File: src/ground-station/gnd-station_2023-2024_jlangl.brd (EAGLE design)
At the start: 114.3 x 54.3 mm, 9 parts, among them IC1 LM7805_TO220V, U1 ADAFRUIT_RFM95W_LORA_RADIO

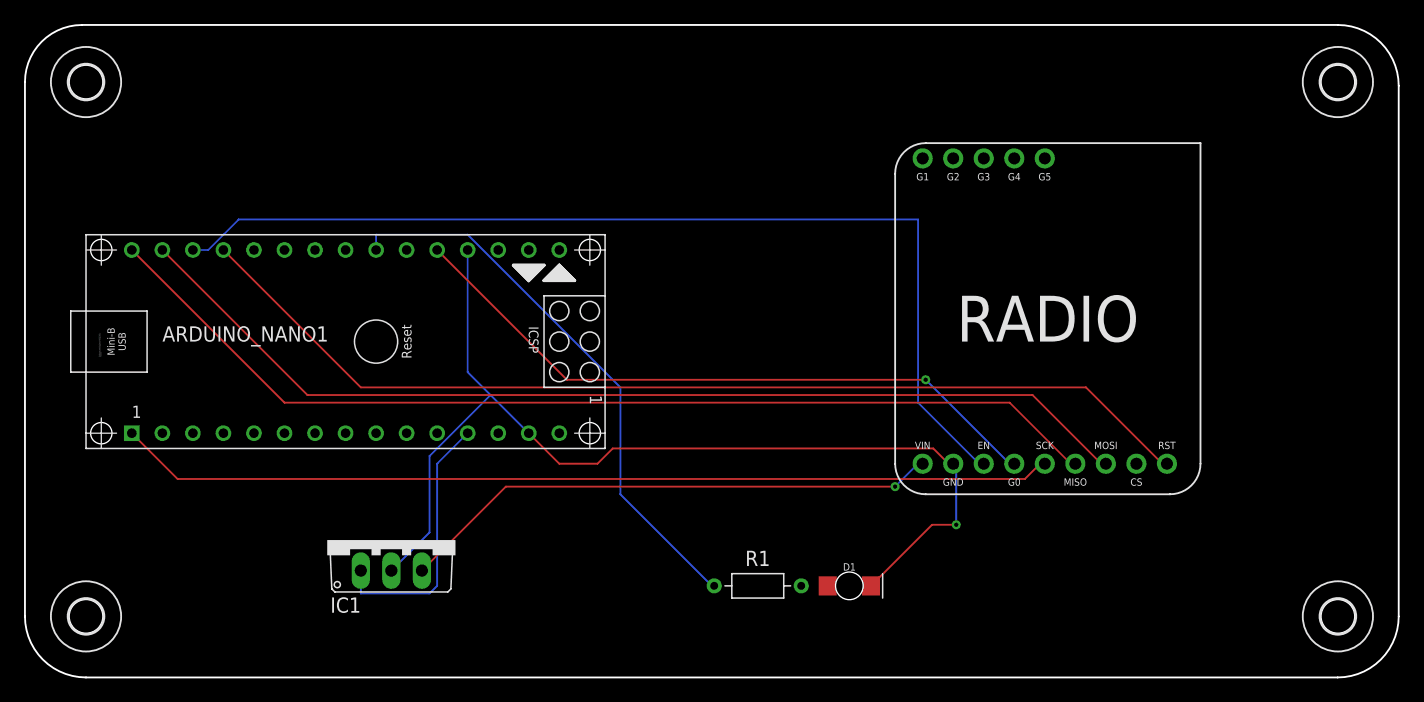
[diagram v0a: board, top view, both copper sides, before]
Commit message: removed 3.3v regulator, spaced out wires
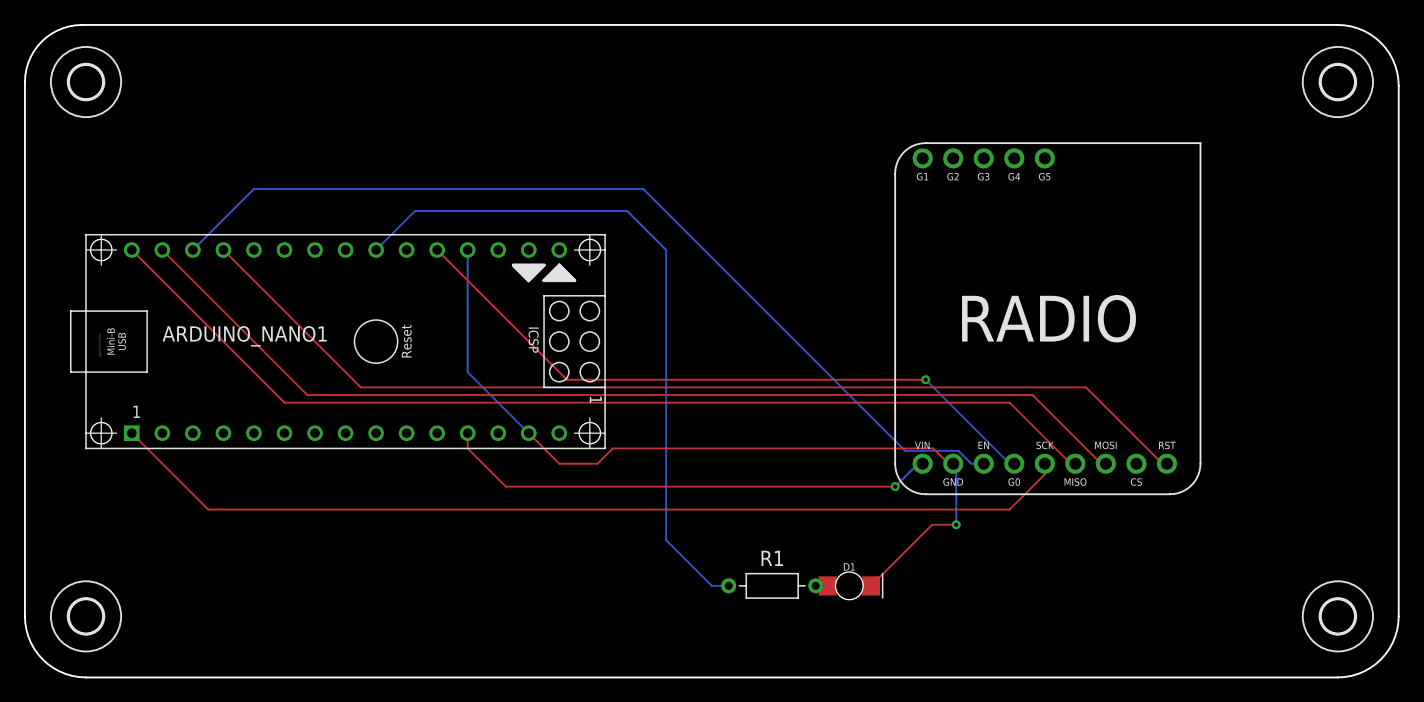
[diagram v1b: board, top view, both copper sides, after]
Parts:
- removed IC1: LM7805_TO220V, IC_Power-Management:TO220V
- moved R1 1.20 mm to (62.2, 7.62)
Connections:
- removed net N$4: ARDUINO_NANO1.12, IC1.1
- net GND: no longer IC1.2
- net LORA3.3V: now also ARDUINO_NANO1.12; no longer IC1.3
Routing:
- net N$4: track 22.3 -> 0.00 mm
- net GND: track 87.2 -> 69.1 mm
- net LED1: track 46.7 -> 57.7 mm
- net EN: track 84.2 -> 77.4 mm
- net LORA3.3V: track 45.3 -> 41.2 mm
- net SCK: track 78.1 -> 80.7 mm
